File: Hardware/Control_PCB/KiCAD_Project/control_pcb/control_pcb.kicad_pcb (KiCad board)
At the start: 4 copper layers, 82.6 x 76.2 mm, 81 parts, among them J1 Conn_01x02, J2 ISP, J3 Spare 2, J5 Micro_SD_Card_Det, J6 Battery, J7 External Switch, SW1 Freq Select, U1 STM32F103CBT6, U2 SN74LVC1G18, U3 TX2M-400-5-NSSL, U4 IF-D96F, U5 TC4S584F, U6 MAX-M8C, U7 LT1521-3.3, U8 MAX3232, Y1 8MHz

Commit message: Control PCB Rev 1.0 complete.
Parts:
- added Q1: BSS138, TO_SOT_Packages_SMD:SOT-23, F.Cu at (134.2, 106.8)
- added R27: 10k, Resistors_SMD:R_0603_HandSoldering, B.Cu at (136.8, 110.0)
- added R28: 10k, Resistors_SMD:R_0603_HandSoldering, F.Cu at (134.2, 104.0)
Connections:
- R18 pad 1: Fiber_Serial_In -> Net-(Q1-Pad3)
- R19 pad 1: Fiber_Serial_In -> Net-(Q1-Pad3)
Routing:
- net Net-(Q1-Pad3): track 0.00 -> 9.83 mm, vias 0 -> 1
- net Fiber_Serial_In: track 45.6 -> 54.8 mm
- net +3V3: track 61.8 -> 64.8 mm, vias 20 -> 21
- net +BATT: track 113.5 -> 115.7 mm

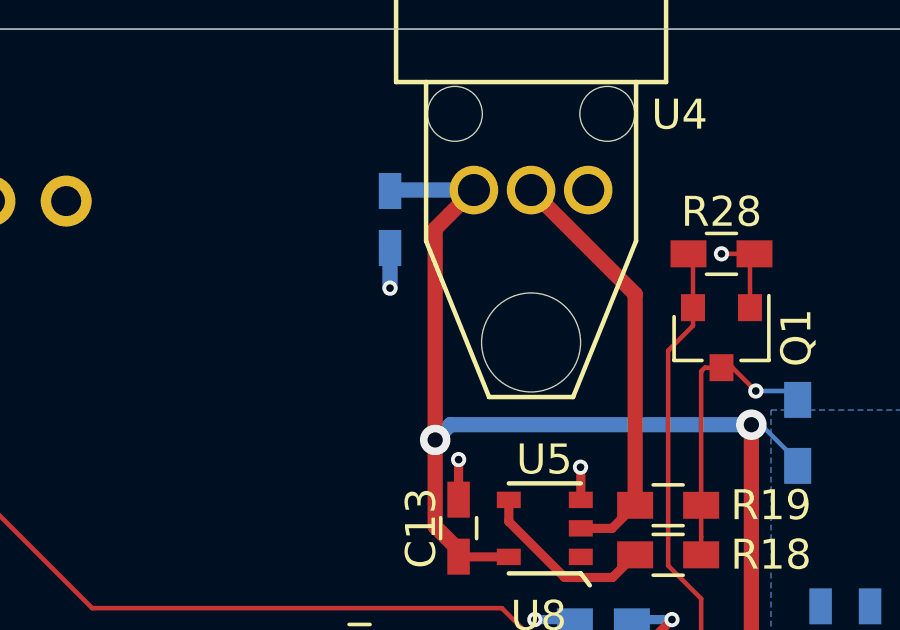
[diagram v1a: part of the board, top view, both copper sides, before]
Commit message: Add pullup to fiber optic receiver. Closes #12.
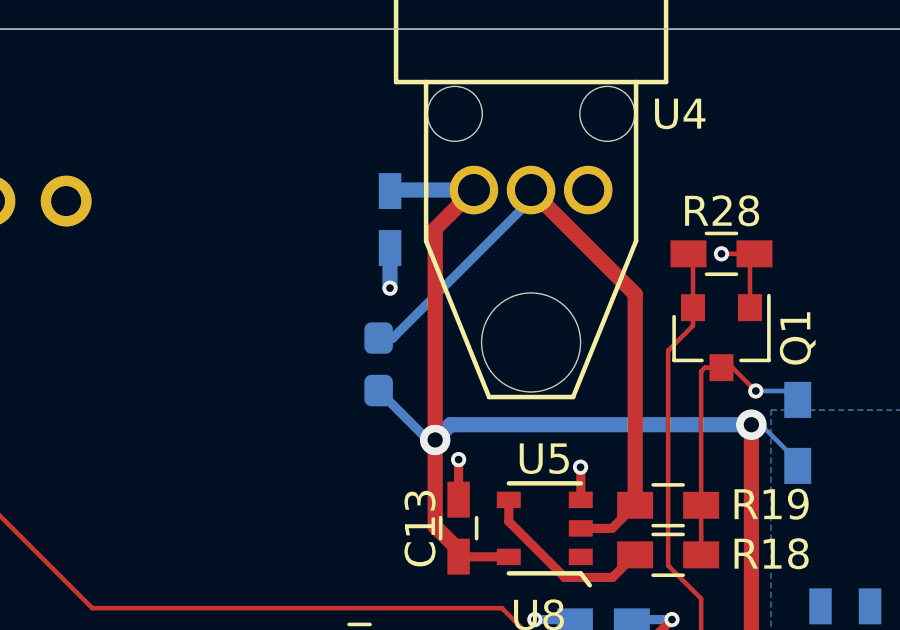
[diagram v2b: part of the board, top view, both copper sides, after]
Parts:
- added R29: 10k, Resistor_SMD:R_0603_1608Metric_Pad1.05x0.95mm_HandSolder, B.Cu at (122.8, 107.7)
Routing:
- net Net-(R19-Pad2): track 14.1 -> 21.4 mm
- net +BATT: track 115.7 -> 118.3 mm
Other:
- board text added: "Data Control Module Rev 2.0 April 2020 P/N 3-0000032"
- board text removed: "Data Control Module Rev 1.0 December 2019 P/N 3-0000022"
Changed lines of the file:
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@@
-(kicad_pcb (version 20171130) (host pcbnew "(5.1.4)-1")
+(kicad_pcb (version 20171130) (host pcbnew "(5.1.5)-3")
   (general
     (thickness 1.6)
     (drawings 8)
-    (tracks 654)
+    (tracks 659)
     (zones 0)
-    (modules 84)
+    (modules 85)
     (nets 56)
   )
@@
   )
   (setup
-    (last_trace_width 0.1524)
+    (last_trace_width 0.3048)
     (user_trace_width 0.1524)
     (user_trace_width 0.3048)
@@
     )
   )
+  (module Resistor_SMD:R_0603_1608Metric_Pad1.05x0.95mm_HandSolder (layer B.Cu)
+    (at 122.809 107.696 90)
+    (descr "Resistor SMD 0603 (1608 Metric), square (rectangular) end terminal, IPC_7351 nominal with elongated pad for handsoldering. (Body size source: http://www.tortai-tech.com/upload/download/2011102023233369053.pdf), generated with kicad-footprint-generator")
+    (tags "resistor handsolder")
+    (attr smd)
+    (fp_text reference R29 (at 0 -1.397 90) (layer B.SilkS)
+      (effects (font (size 1 1) (thickness 0.15)) (justify mirror))
+    )
+    (fp_text value 10k (at 0 -1.43 90) (layer B.Fab)
+      (effects (font (size 1 1) (thickness 0.15)) (justify mirror))
+    )
+    (fp_line (start -0.8 -0.4) (end -0.8 0.4) (layer B.Fab) (width 0.1))
+    (fp_line (start -0.8 0.4) (end 0.8 0.4) (layer B.Fab) (width 0.1))
+    (fp_line (start 0.8 0.4) (end 0.8 -0.4) (layer B.Fab) (width 0.1))
+    (fp_line (start 0.8 -0.4) (end -0.8 -0.4) (layer B.Fab) (width 0.1))
+    (fp_line (start -0.171267 0.51) (end 0.171267 0.51) (layer B.SilkS) (width 0.12))
+    (fp_line (start -0.171267 -0.51) (end 0.171267 -0.51) (layer B.SilkS) (width 0.12))
+    (fp_line (start -1.65 -0.73) (end -1.65 0.73) (layer B.CrtYd) (width 0.05))
+    (fp_line (start -1.65 0.73) (end 1.65 0.73) (layer B.CrtYd) (width 0.05))
+    (fp_line (start 1.65 0.73) (end 1.65 -0.73) (layer B.CrtYd) (width 0.05))
+    (fp_line (start 1.65 -0.73) (end -1.65 -0.73) (layer B.CrtYd) (width 0.05))
+    (fp_text user %R (at 0 0 90) (layer B.Fab)
+      (effects (font (size 0.4 0.4) (thickness 0.06)) (justify mirror))
+    )
+    (pad 1 smd roundrect (at -0.875 0 90) (size 1.05 0.95) (layers B.Cu B.Paste B.Mask) (roundrect_rratio 0.25)
+      (net 9 +BATT))
+    (pad 2 smd roundrect (at 0.875 0 90) (size 1.05 0.95) (layers B.Cu B.Paste B.Mask) (roundrect_rratio 0.25)
+      (net 34 "Net-(R19-Pad2)"))
+    (model ${KISYS3DMOD}/Resistor_SMD.3dshapes/R_0603_1608Metric.wrl
+      (at (xyz 0 0 0))
+      (scale (xyz 1 1 1))
+      (rotate (xyz 0 0 0))
+    )
+  )
   (gr_text FREQ (at 144.272 167.513) (layer F.SilkS)
     (effects (font (size 1.5 1.5) (thickness 0.3)))
   )
-  (gr_text "Data Control Module\nRev 1.0 December 2019\nP/N 3-0000022" (at 141.859 105.537) (layer B.SilkS)
+  (gr_text "Data Control Module\nRev 2.0 April 2020\nP/N 3-0000032" (at 141.859 105.537) (layer B.SilkS)
     (effects (font (size 0.9906 0.9906) (thickness 0.24765)) (justify mirror))
   )
@@
   (segment (start 142.918 161.247) (end 141.732 161.247) (width 0.1524) (layer B.Cu) (net 8) (status 20))
   (segment (start 143.6696 161.247) (end 142.918 161.247) (width 0.1524) (layer B.Cu) (net 8))
-  (segment (start 135.189 104.163) (end 135.339 104.013) (width 0.1524) (layer F.Cu) (net 8))
-  (segment (start 135.189 105.807) (end 135.189 104.163) (width 0.1524) (layer F.Cu) (net 8))
+  (segment (start 135.189 104.163) (end 135.339 104.013) (width 0.1524) (layer F.Cu) (net 8) (status 30))
+  (segment (start 135.189 105.807) (end 135.189 104.163) (width 0.1524) (layer F.Cu) (net 8) (status 30))
   (via (at 134.239 104.013) (size 0.508) (drill 0.254) (layers F.Cu B.Cu) (net 8))
-  (segment (start 135.339 104.013) (end 134.239 104.013) (width 0.1524) (layer F.Cu) (net 8))
+  (segment (start 135.339 104.013) (end 134.239 104.013) (width 0.1524) (layer F.Cu) (net 8) (status 10))
   (segment (start 125.483001 114.114001) (end 125.476 114.107) (width 0.3048) (layer F.Cu) (net 9) (status 30))
   (segment (start 127.15 114.114001) (end 125.483001 114.114001) (width 0.3048) (layer F.Cu) (net 9) (status 30))
@@
   (segment (start 117.465 128.768) (end 118.877401 127.355599) (width 1.27) (layer In2.Cu) (net 9))
   (segment (start 135.5556 109.7086) (end 135.2356 109.7086) (width 0.1524) (layer B.Cu) (net 9))
-  (segment (start 136.779 110.932) (end 135.5556 109.7086) (width 0.1524) (layer B.Cu) (net 9))
-  (segment (start 136.779 111.082) (end 136.779 110.932) (width 0.1524) (layer B.Cu) (net 9))
+  (segment (start 136.779 110.932) (end 135.5556 109.7086) (width 0.1524) (layer B.Cu) (net 9) (status 10))
+  (segment (start 136.779 111.082) (end 136.779 110.932) (width 0.1524) (layer B.Cu) (net 9) (status 30))
+  (segment (start 124.454599 110.216599) (end 122.809 108.571) (width 0.3048) (layer B.Cu) (net 9))
+  (segment (start 124.694599 110.216599) (end 124.454599 110.216599) (width 0.3048) (layer B.Cu) (net 9))
   (segment (start 101.981 154.866) (end 101.983 154.864) (width 0.34798) (layer F.Cu) (net 10) (status 30))
   (segment (start 101.981 157.927) (end 101.981 154.866) (width 0.34798) (layer F.Cu) (net 10) (status 30))
@@
   (segment (start 137.922 146.634) (end 137.966 146.59) (width 0.1524) (layer F.Cu) (net 32) (status 30))
   (segment (start 137.922 149.352) (end 137.922 146.634) (width 0.1524) (layer F.Cu) (net 32) (status 20))
-  (segment (start 133.289 104.163) (end 133.139 104.013) (width 0.1524) (layer F.Cu) (net 32))
-  (segment (start 133.289 105.807) (end 133.289 104.163) (width 0.1524) (layer F.Cu) (net 32))
+  (segment (start 133.289 104.163) (end 133.139 104.013) (width 0.1524) (layer F.Cu) (net 32) (status 30))
+  (segment (start 133.289 105.807) (end 133.289 104.163) (width 0.1524) (layer F.Cu) (net 32) (status 30))
   (segment (start 133.561 115.507482) (end 132.461 114.407482) (width 0.1524) (layer F.Cu) (net 32))
   (segment (start 133.561 130.90767) (end 133.561 115.507482) (width 0.1524) (layer F.Cu) (net 32))
-  (segment (start 133.289 106.4094) (end 133.289 105.807) (width 0.1524) (layer F.Cu) (net 32))
+  (segment (start 133.289 106.4094) (end 133.289 105.807) (width 0.1524) (layer F.Cu) (net 32) (status 20))
   (segment (start 132.461 107.2374) (end 133.289 106.4094) (width 0.1524) (layer F.Cu) (net 32))
   (segment (start 132.461 114.407482) (end 132.461 107.2374) (width 0.1524) (layer F.Cu) (net 32))
@@
   (segment (start 131.361 105.356) (end 127.892001 101.887001) (width 0.508) (layer F.Cu) (net 34) (status 20))
   (segment (start 131.361 112.395) (end 131.361 105.356) (width 0.508) (layer F.Cu) (net 34) (status 10))
+  (segment (start 123.284 106.821) (end 127.892001 102.212999) (width 0.3048) (layer B.Cu) (net 34))
+  (segment (start 127.892001 102.212999) (end 127.892001 101.887001) (width 0.3048) (layer B.Cu) (net 34))
+  (segment (start 122.809 106.821) (end 123.284 106.821) (width 0.3048) (layer B.Cu) (net 34))
   (segment (start 106.383 142.662) (end 106.045 142.324) (width 0.3048) (layer F.Cu) (net 35) (status 30))
   (segment (start 106.383 145.364) (end 106.383 142.662) (width 0.3048) (layer F.Cu) (net 35) (status 30))
@@
   (segment (start 146.939 157.48) (end 146.939 155.824) (width 0.1524) (layer F.Cu) (net 54) (status 20))
   (via (at 135.382 108.585) (size 0.508) (drill 0.254) (layers F.Cu B.Cu) (net 55))
-  (segment (start 134.239 107.807) (end 134.604 107.807) (width 0.1524) (layer F.Cu) (net 55))
-  (segment (start 134.604 107.807) (end 135.382 108.585) (width 0.1524) (layer F.Cu) (net 55))
-  (segment (start 136.482 108.585) (end 136.779 108.882) (width 0.1524) (layer B.Cu) (net 55))
-  (segment (start 135.382 108.585) (end 136.482 108.585) (width 0.1524) (layer B.Cu) (net 55))
-  (segment (start 133.561 113.4436) (end 133.561 112.395) (width 0.1524) (layer F.Cu) (net 55))
-  (segment (start 133.561 114.046) (end 133.561 113.4436) (width 0.1524) (layer F.Cu) (net 55))
-  (segment (start 133.6866 107.807) (end 134.239 107.807) (width 0.1524) (layer F.Cu) (net 55))
+  (segment (start 134.239 107.807) (end 134.604 107.807) (width 0.1524) (layer F.Cu) (net 55) (status 30))
+  (segment (start 134.604 107.807) (end 135.382 108.585) (width 0.1524) (layer F.Cu) (net 55) (status 10))
+  (segment (start 136.482 108.585) (end 136.779 108.882) (width 0.1524) (layer B.Cu) (net 55) (status 30))
+  (segment (start 135.382 108.585) (end 136.482 108.585) (width 0.1524) (layer B.Cu) (net 55) (status 20))
+  (segment (start 133.561 113.4436) (end 133.561 112.395) (width 0.1524) (layer F.Cu) (net 55) (status 20))
+  (segment (start 133.561 114.046) (end 133.561 113.4436) (width 0.1524) (layer F.Cu) (net 55) (status 10))
+  (segment (start 133.6866 107.807) (end 134.239 107.807) (width 0.1524) (layer F.Cu) (net 55) (status 20))
   (segment (start 133.561 107.9326) (end 133.6866 107.807) (width 0.1524) (layer F.Cu) (net 55))
-  (segment (start 133.561 112.395) (end 133.561 107.9326) (width 0.1524) (layer F.Cu) (net 55))
+  (segment (start 133.561 112.395) (end 133.561 107.9326) (width 0.1524) (layer F.Cu) (net 55) (status 10))
   (zone (net 2) (net_name GND) (layer In1.Cu) (hatch edge 0.508)
     (connect_pads (clearance 0.508))
